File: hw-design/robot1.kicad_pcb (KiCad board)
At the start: 2 copper layers, 49.7 x 26.7 mm, 111 parts, among them P1 CONN_01X17, P2 CONN_01X17, P3 CONN_01X03, P4 left_motor, P5 right_motor, P6 CONN_01X17, P7 CONN_01X17, P8 CONN_01X17, P9 CONN_01X17, Q1 BC847, Q2 BC847, Q3 BC847, Q4 BC847, Q5 BC847, Q6 BC847, Q7 BC847, SW1 SWITCH_INV, U1 usb-micro, U10 China-0038, U11 China-0038, U12 China-0038, U13 China-0038, U14 STM32F030CxTx, U2 TCS3472, U3 MCP73833, U4 MIC5501, U5 drv8835, U6 drv8835, U7 BlueNRG, U8 BALF-NRG-01D3, U9 TCS3472, Y1 16MHz, Y2 32kHz, Y3 16MHz

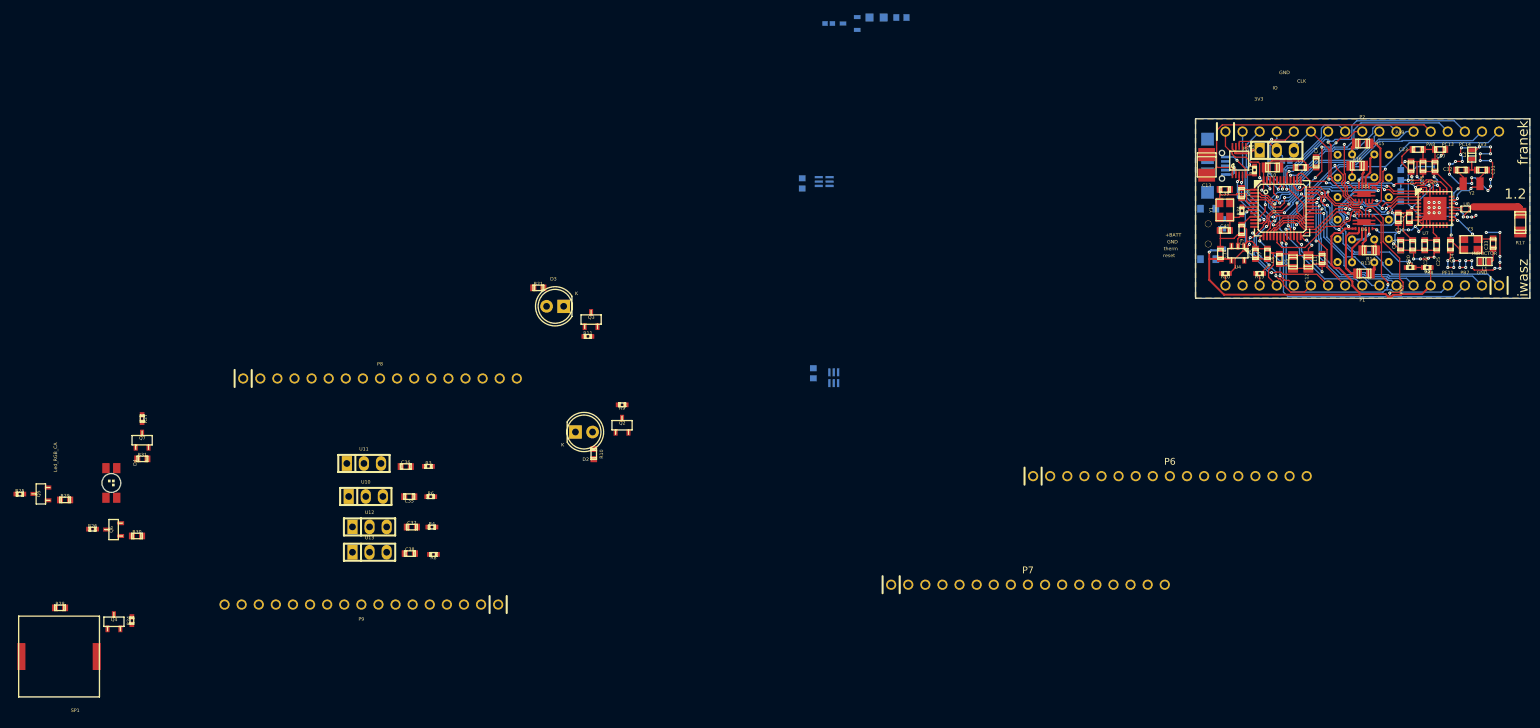
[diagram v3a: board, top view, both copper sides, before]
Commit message: 2 boards and 1 little with color sensors.
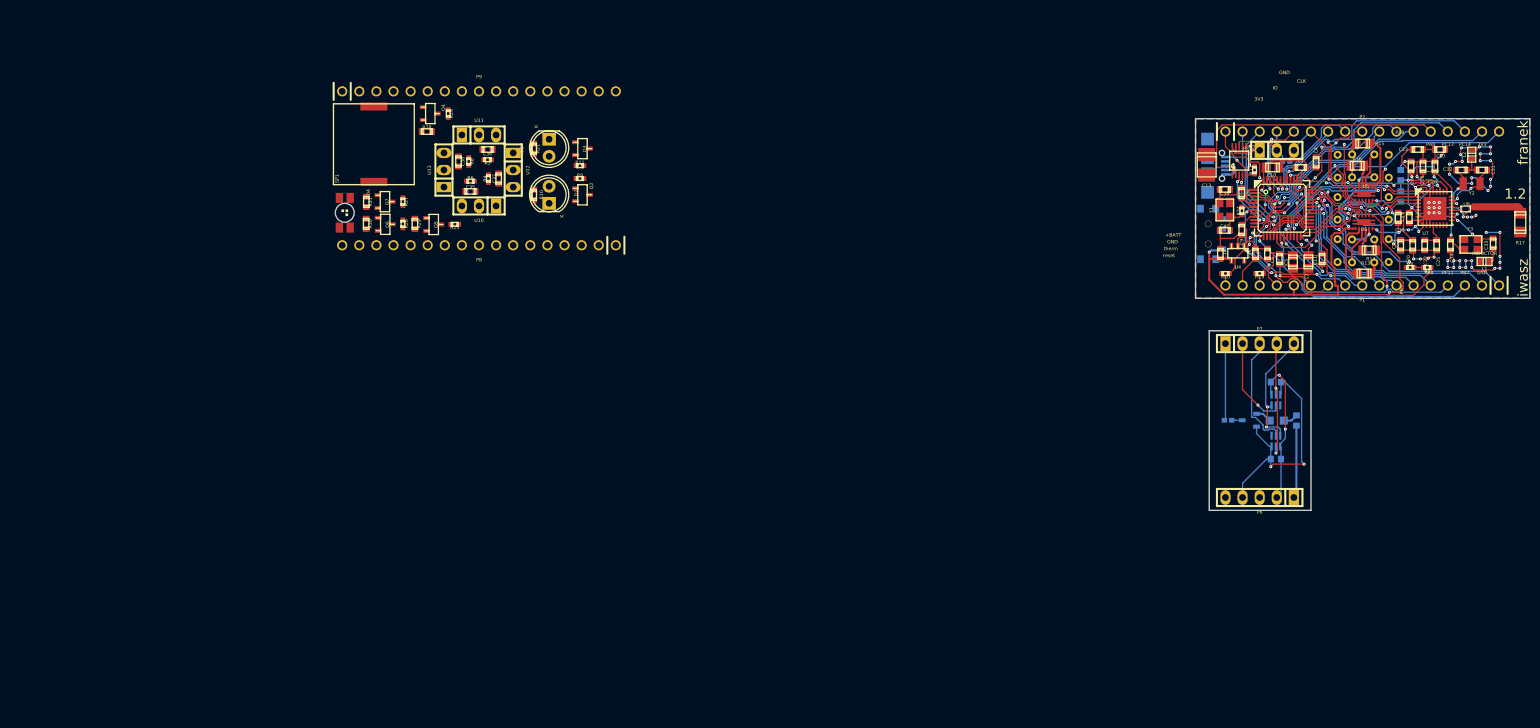
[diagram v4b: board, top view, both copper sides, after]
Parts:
- P6, P7: value CONN_01X17 -> CONN_01X05; footprint iwasz:pin_socket_17 -> w_pin_strip:pin_strip_5
- moved R28 89.3 mm to (37.6, 117.5)
- moved Q4 88.9 mm to (38.1, 114.8), turned to 270 degrees
- moved R24 88.8 mm to (40.8, 114.8), turned to 270 degrees
- moved SP1 88.8 mm to (29.7, 119.8), turned to 270 degrees
- moved D1 84.4 mm to (163.8, 160.4)
- moved R2 83.8 mm to (166.8, 160.4), turned to 90 degrees
- moved R1 83.6 mm to (156.6, 160.4)
- moved Q1 83.6 mm to (159.8, 160.4)
- moved P9 78.2 mm to (45.3, 111.5), turned to 0 degrees
- moved C2 76.3 mm to (163.7, 154.7), turned to 0 degrees
- moved R25 76.0 mm to (41.7, 131.3), turned to 180 degrees
- moved U2 74.5 mm to (163.7, 157.4), turned to 0 degrees
- moved Q5 70.8 mm to (38.6, 131.3), turned to 270 degrees
- moved C3 69.9 mm to (163.7, 166.1), turned to 180 degrees
- moved U9 66.3 mm to (163.7, 163.4), turned to 180 degrees
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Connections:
- C2 pad 1: GND -> GNDD
- C2 pad 2: +3V3 -> +3.3VA
- C3 pad 1: GND -> GNDD
- C3 pad 2: +3V3 -> +3.3VA
- P1 pad 10: /micro/ir_sense -> /micro/nrst
- P1 pad 11: /micro/nrst -> /micro/console_tx
- P1 pad 12: /micro/console_tx -> /micro/console_rx
- P1 pad 13: /micro/console_rx -> +BATT
- P1 pad 5: +BATT -> /micro/led_b
- P1 pad 6: /micro/led_b -> /micro/led_g
- P1 pad 7: /micro/led_g -> /micro/led_r
- P1 pad 8: /micro/led_r -> /micro/ir_cannon
- P1 pad 9: /micro/ir_cannon -> /micro/ir_sense
- P6 pad 1: Net-(P6-Pad1) -> VCC
- P6 pad 2: Net-(P6-Pad2) -> +3.3VA
- P6 pad 4: Net-(P6-Pad4) -> GNDD
- P6 pad 5: +BATT -> Net-(P6-Pad5)
- P8 pad 13: Net-(P8-Pad13) -> VAA
- P8 pad 5: VAA -> Net-(P8-Pad5)
- Q1 pad 3: GND -> GNDD
- R2 pad 2: +BATT -> VCC
- U2 pad 1: +3V3 -> +3.3VA
- U2 pad 3: GND -> GNDD
- U9 pad 1: +3V3 -> +3.3VA
- U9 pad 3: GND -> GNDD
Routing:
- net GNDD: track 0.00 -> 35.9 mm, vias 0 -> 2
- net +3.3VA: track 0.00 -> 22.8 mm, vias 0 -> 2
- net /photo/scl: track 0.00 -> 18.5 mm, vias 0 -> 2
- net /photo/sda: track 0.00 -> 18.2 mm, vias 0 -> 2
- net /photo/photo_r_int: track 0.00 -> 17.1 mm
- net /photo/photo_l_int: track 0.00 -> 13.9 mm, vias 0 -> 1
- net /photo/photo_illumination: track 0.00 -> 11.5 mm
- net VCC: track 0.00 -> 10.8 mm
- net GND: track 177.2 -> 181.9 mm
- net /micro/console_tx: track 16.1 -> 19.1 mm
- net /micro/ir_sense: track 15.5 -> 18.4 mm, vias 2 -> 3
- net /micro/ir_cannon: track 24.5 -> 27.4 mm
- net /micro/nrst: track 21.4 -> 24.0 mm, vias 2 -> 3
- net /micro/console_rx: track 10.2 -> 12.8 mm
- net /micro/led_g: track 21.9 -> 24.4 mm
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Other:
- board size 49.7 x 26.7 mm -> 49.7 x 58.2 mm

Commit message: Hard work on the 1.2 PCB
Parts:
- moved Q2 0.51 mm to (60.7, 126.4)
- moved R10 0.51 mm to (53.5, 126.4)
- moved R11 0.51 mm to (60.3, 122.0)
- moved D2 0.51 mm to (55.8, 127.6)
- moved D3 0.51 mm to (55.8, 118.1)
- moved Q3 0.51 mm to (60.7, 119.5)
- moved R21 0.51 mm to (53.5, 119.5)
- moved R9 0.51 mm to (60.3, 124.0)
- moved C35 0.38 mm to (44.1, 126.0)
- moved C36 0.38 mm to (46.6, 119.8)
- moved C37 0.38 mm to (48.3, 124.1)
- moved C38 0.38 mm to (42.3, 121.5)
- moved R3 0.38 mm to (46.6, 121.3)
- moved R4 0.38 mm to (46.7, 124.1)
- moved R6 0.38 mm to (44.1, 124.5)
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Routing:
- net GNDA: track 0.00 -> 91.8 mm, vias 0 -> 10
- net +3.3VP: track 0.00 -> 65.3 mm, vias 0 -> 1
- net GND: track 181.9 -> 229.2 mm, vias 64 -> 74
- net /peripherals/ir_sense: track 0.00 -> 44.3 mm
- net VAA: track 0.00 -> 27.5 mm, vias 0 -> 1
- net /peripherals/ir_cannon: track 0.00 -> 26.2 mm, vias 0 -> 1
- net /peripherals/led_b: track 0.00 -> 21.8 mm
- net /peripherals/led_g: track 0.00 -> 18.7 mm
- net Net-(P3-Pad1): track 6.10 -> 24.4 mm, vias 0 -> 1
- net Net-(Q4-Pad1): track 0.00 -> 16.0 mm
- net Net-(D4-Pad2): track 0.00 -> 12.7 mm, vias 0 -> 2
- net /peripherals/led_r: track 0.00 -> 6.88 mm
- net +3V3: track 133.2 -> 139.9 mm, vias 14 -> 15
- net Net-(D2-Pad1): track 0.00 -> 5.17 mm
- net Net-(D3-Pad1): track 0.00 -> 4.08 mm
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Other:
- board text added: "+5V"
- board text added: "BATT"
- board text added: "IRC"
- board text added: "IRS"
- board text added: "LEDB"
- board text added: "LEDG"
- board text added: "LEDR"
- board text added: "PB14"
- board text added: "PB15"
- board text added: "PC15"
- board text added: "RX"
- board text added: "TX"
- board text added: "VBAT"
- board text added: "aen.L"
- board text added: "aen.R"
- board text added: "aph.L"
- board text added: "aph.R"
- board text added: "ben.L"
- board text added: "ben.R"
- board text added: "bph.L"
- board text added: "bph.R"
- board text added: "illum"
- board text added: "l.int"
- board text added: "nrst"
- board text added: "r.int"
- board text added: "scl"
- board text added: "sda"
- board text added: "sound"
- board text removed: "+BATT"
- board text removed: "PA8"
- board text removed: "PA9"
- board text removed: "PB7"
- board text removed: "PB8"
- board text removed: "PB9"
- board text removed: "PF11"
- board text removed: "reset"

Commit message: PCB 1.2 almost done, only shape could be improved.
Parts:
- L1, L2: footprint w_smd_inductors:inductor_smd_0603 -> w_smd_cap:c_0603
- moved D4 169.6 mm to (192.7, 101.9), turned to 0 degrees
- moved R30 163.9 mm to (189.5, 100.3), turned to 90 degrees
- moved R31 162.8 mm to (189.5, 103.5), turned to 90 degrees
- moved SP1 161.4 mm to (188.8, 92.3)
- moved Q6 158.4 mm to (186.7, 100.2), turned to 90 degrees
- moved Q7 157.3 mm to (186.8, 103.6), turned to 90 degrees
- moved R26 153.2 mm to (184.1, 100.3), turned to 90 degrees
- moved R27 152.0 mm to (184.1, 103.6), turned to 90 degrees
- moved R29 148.8 mm to (182.1, 103.7), turned to 90 degrees
- moved R28 146.7 mm to (181.0, 86.6), turned to 180 degrees
- moved Q4 144.7 mm to (180.5, 89.2), turned to 90 degrees
- moved Q5 143.3 mm to (179.3, 103.6), turned to 90 degrees
- moved R24 140.6 mm to (178.6, 87.0)
- moved U13 140.5 mm to (178.0, 95.6), turned to 270 degrees
- moved R25 137.2 mm to (176.1, 103.6), turned to 0 degrees
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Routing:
- net GND: track 229.2 -> 403.7 mm, vias 74 -> 187
- net GNDA: track 91.8 -> 210.7 mm, vias 10 -> 86
- net GNDD: track 35.9 -> 80.4 mm, vias 2 -> 36
- net VAA: track 27.5 -> 44.8 mm, vias 1 -> 2
- net /peripherals/led_b: track 21.8 -> 4.94 mm
- net /peripherals/sound: track 2.96 -> 11.9 mm
- net /peripherals/led_g: track 18.7 -> 10.6 mm
- net /peripherals/ir_cannon: track 26.2 -> 21.2 mm
- net /micro/aphasel: track 42.5 -> 47.4 mm
- net +3.3VP: track 65.3 -> 69.1 mm, vias 1 -> 0
- net /peripherals/led_r: track 6.88 -> 3.48 mm
- net /micro/aenblr: track 46.4 -> 49.2 mm
- net Net-(R5-Pad1): track 24.2 -> 26.8 mm
- net /micro/console_rx: track 12.9 -> 14.8 mm
- net /micro/bphaser: track 46.2 -> 47.9 mm
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- added copper zone on B.Cu, net GNDA
- added copper zone on F.Cu, net GNDA
- added copper zone on B.Cu, net GNDD
- added copper zone on F.Cu, net GNDD
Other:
- board size 49.7 x 58.2 mm -> 114.4 x 26.7 mm
- board text added: "*"
- board text added: "PCB thickness : 1mm"

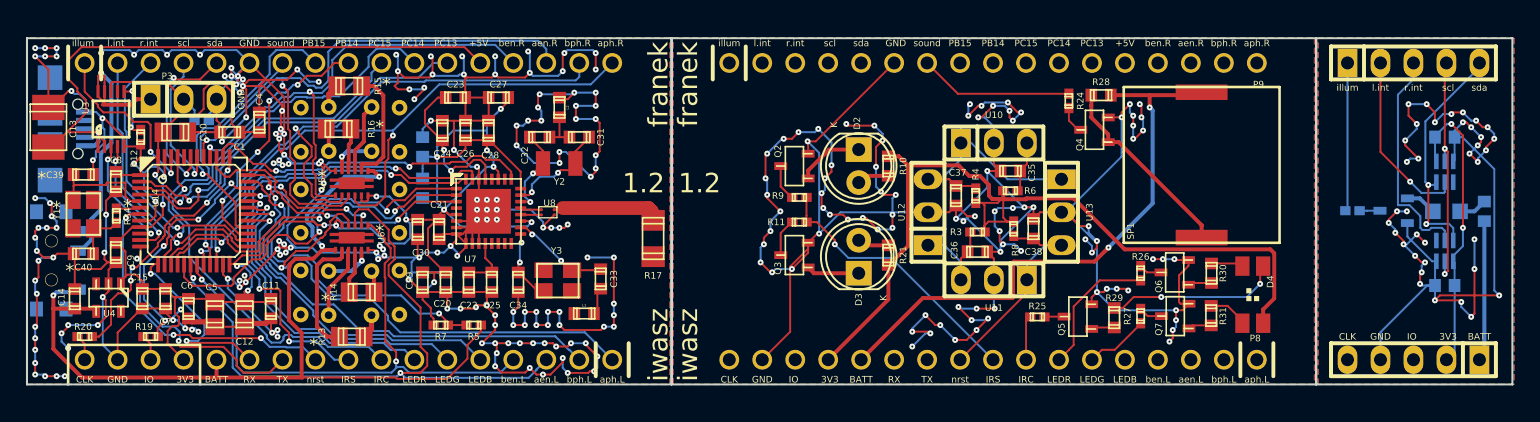
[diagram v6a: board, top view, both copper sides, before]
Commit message: PCB shape improved
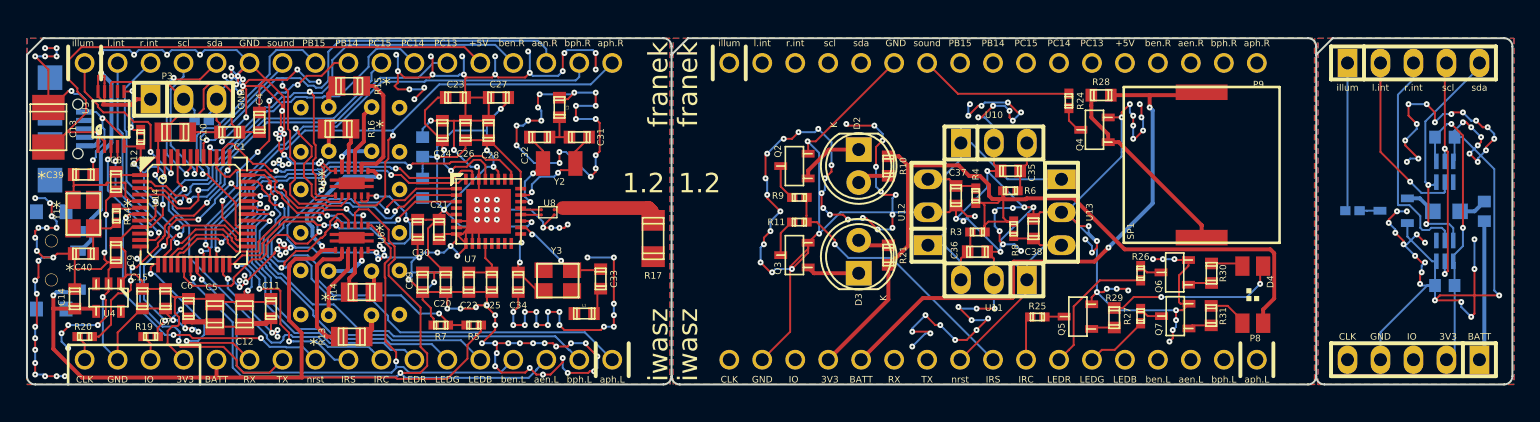
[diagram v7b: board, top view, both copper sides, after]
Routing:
- net GND: track 403.7 -> 402.9 mm, vias 187 -> 186
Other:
- outline, holes or cut-outs redrawn
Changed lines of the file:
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@@
     (links 274)
     (no_connects 0)
-    (area 81.385534 68.06 212.8774 120.488545)
+    (area 98.222999 82.093999 212.800001 108.914001)
     (thickness 1.6)
-    (drawings 197)
-    (tracks 2718)
+    (drawings 209)
+    (tracks 2716)
     (zones 0)
     (modules 111)
@@
     )
   )
+  (gr_arc (start 147.32 108.204) (end 147.955 108.204) (angle 90) (layer Edge.Cuts) (width 0.15))
+  (gr_arc (start 148.59 108.204) (end 148.59 108.839) (angle 90) (layer Edge.Cuts) (width 0.15))
+  (gr_arc (start 196.977 108.204) (end 197.612 108.204) (angle 90) (layer Edge.Cuts) (width 0.15))
+  (gr_arc (start 198.247 108.204) (end 198.247 108.839) (angle 90) (layer Edge.Cuts) (width 0.15))
+  (gr_arc (start 212.09 108.204) (end 212.725 108.204) (angle 90) (layer Edge.Cuts) (width 0.15))
+  (gr_arc (start 212.09 82.804) (end 212.09 82.169) (angle 90) (layer Edge.Cuts) (width 0.15))
+  (gr_arc (start 196.977 82.804) (end 196.977 82.169) (angle 90) (layer Edge.Cuts) (width 0.15))
+  (gr_arc (start 147.32 82.804) (end 147.32 82.169) (angle 90) (layer Edge.Cuts) (width 0.15))
+  (gr_line (start 197.612 83.439) (end 197.612 82.804) (layer Edge.Cuts) (width 0.15))
+  (gr_line (start 147.955 83.439) (end 147.955 82.804) (layer Edge.Cuts) (width 0.15))
+  (gr_line (start 147.955 83.439) (end 149.225 82.169) (layer Edge.Cuts) (width 0.15))
+  (gr_line (start 197.612 83.439) (end 198.882 82.169) (layer Edge.Cuts) (width 0.15))
+  (gr_line (start 98.298 83.439) (end 99.568 82.169) (layer Edge.Cuts) (width 0.15))
+  (gr_arc (start 98.933 108.204) (end 98.933 108.839) (angle 90) (layer Edge.Cuts) (width 0.15))
   (gr_line (start 101.473 105.791) (end 101.473 108.839) (layer F.SilkS) (width 0.2))
   (gr_line (start 111.633 105.791) (end 111.633 108.839) (layer F.SilkS) (width 0.2))
@@
     (effects (font (size 1.5 1.5) (thickness 0.3)))
   )
-  (gr_line (start 147.955 82.169) (end 147.955 108.839) (layer Edge.Cuts) (width 0.15))
-  (gr_line (start 147.955 82.169) (end 197.612 82.169) (layer Edge.Cuts) (width 0.15))
-  (gr_line (start 147.955 108.839) (end 197.612 108.839) (layer Edge.Cuts) (width 0.15))
-  (gr_line (start 197.612 82.169) (end 197.612 108.839) (layer Edge.Cuts) (width 0.15))
+  (gr_line (start 149.225 82.169) (end 196.977 82.169) (layer Edge.Cuts) (width 0.15))
+  (gr_line (start 148.59 108.839) (end 196.977 108.839) (layer Edge.Cuts) (width 0.15))
   (gr_text * (at 129.667 89.789) (layer B.SilkS)
     (effects (font (size 1.016 1.016) (thickness 0.1016)) (justify mirror))
@@
     (effects (font (size 0.508 0.508) (thickness 0.0508)))
   )
-  (gr_line (start 212.725 82.169) (end 212.725 108.839) (layer Edge.Cuts) (width 0.15))
-  (gr_line (start 197.612 82.169) (end 212.725 82.169) (layer Edge.Cuts) (width 0.15))
-  (gr_line (start 197.612 108.839) (end 212.725 108.839) (layer Edge.Cuts) (width 0.15))
-  (gr_line (start 197.612 82.169) (end 197.612 108.839) (layer Edge.Cuts) (width 0.15))
+  (gr_line (start 212.725 82.804) (end 212.725 108.204) (layer Edge.Cuts) (width 0.15))
+  (gr_line (start 198.882 82.169) (end 212.09 82.169) (layer Edge.Cuts) (width 0.15))
+  (gr_line (start 198.247 108.839) (end 212.09 108.839) (layer Edge.Cuts) (width 0.15))
+  (gr_line (start 197.612 83.439) (end 197.612 108.204) (layer Edge.Cuts) (width 0.15))
   (dimension 6.096 (width 0.3) (layer Dwgs.User)
     (gr_text "6,096 mm" (at 199.31 95.523995 90) (layer Dwgs.User)
@@
     (effects (font (size 0.508 0.508) (thickness 0.0508)) (justify mirror))
   )
-  (gr_line (start 147.955 82.169) (end 147.955 108.839) (layer Edge.Cuts) (width 0.15))
-  (gr_line (start 98.298 108.839) (end 147.955 108.839) (layer Edge.Cuts) (width 0.15))
-  (gr_line (start 98.298 82.169) (end 147.955 82.169) (layer Edge.Cuts) (width 0.15))
+  (gr_line (start 147.955 83.439) (end 147.955 108.204) (layer Edge.Cuts) (width 0.15))
+  (gr_line (start 98.933 108.839) (end 147.32 108.839) (layer Edge.Cuts) (width 0.15))
+  (gr_line (start 99.568 82.169) (end 147.32 82.169) (layer Edge.Cuts) (width 0.15))
   (dimension 26.67 (width 0.3) (layer Dwgs.User)
     (gr_text "26,670 mm" (at 88.035534 95.583775 270) (layer Dwgs.User)
@@
     (arrow2b (pts (xy 89.385534 82.248775) (xy 89.971955 83.375279)))
   )
-  (gr_line (start 98.298 82.169) (end 98.298 108.839) (layer Edge.Cuts) (width 0.15))
+  (gr_line (start 98.298 83.439) (end 98.298 108.204) (layer Edge.Cuts) (width 0.15))
   (segment (start 121.203722 96.571546) (end 122.094027 96.571546) (width 0.1524) (layer B.Cu) (net 1))
   (segment (start 124.805911 96.824251) (end 122.346732 96.824251) (width 0.1524) (layer B.Cu) (net 1))
@@
   (segment (start 100.622418 98.767582) (end 100.33 99.06) (width 0.1524) (layer F.Cu) (net 2))
   (via (at 100.33 99.06) (size 0.4572) (drill 0.1524) (layers F.Cu B.Cu) (net 2))
-  (segment (start 99.695 82.931) (end 98.933 82.931) (width 0.1524) (layer B.Cu) (net 2))
-  (via (at 98.933 82.931) (size 0.4572) (drill 0.1524) (layers F.Cu B.Cu) (net 2))
   (segment (start 100.584 82.931) (end 99.695 82.931) (width 0.1524) (layer F.Cu) (net 2))
   (via (at 99.695 82.931) (size 0.4572) (drill 0.1524) (layers F.Cu B.Cu) (net 2))
